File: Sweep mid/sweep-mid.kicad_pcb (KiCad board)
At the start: 2 copper layers, 229.5 x 95.2 mm, 62 parts, among them J1 AudioJack4dpb, J2 AudioJack4dpb, SW10 SW_Push, SW11 SW_Push, SW11_r1 SW_Push, SW12 SW_Push, SW12_r1 SW_Push, SW13_r1 SW_Push, SW14 SW_Push, SW15 SW_Push, SW15_r1 SW_Push, SW16 SW_Push, SW16_r1 SW_Push, SW17 SW_Push, SW17_r1 SW_Push, SW18 SW_Push, SW18_r1 SW_Push, SW2 SW_Push, SW2 SW_SPDT, SW20 SW_Push, SW20_r1 SW_Push, SW21 SW_Push, SW21_r1 SW_Push, SW2_r1 SW_Push, SW3 SW_Push, SW3_r1 SW_Push, SW4 SW_Push, SW4_r1 SW_Push, SW5 SW_Push, SW5_r1 SW_Push, SW6 SW_Push, SW6_r1 SW_Push, SW7_r1 SW_Push, SW8 SW_Push, SW8_r1 SW_Push, SW9 SW_Push, SW9_r1 SW_Push, U1 ProMicro-kbd, U2 ProMicro-kbd

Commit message: simplify footprint
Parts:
- SW10, SW11, SW11_r1, SW12, SW12_r1, SW13_r1, SW14, SW15, SW15_r1, SW16, SW16_r1, SW17, SW17_r1, SW18, SW18_r1, SW2, SW20, SW20_r1, SW21, SW21_r1, SW2_r1, SW3, SW3_r1, SW4, SW4_r1, SW5, SW5_r1, SW6, SW6_r1, SW7_r1, SW8, SW8_r1, SW9, SW9_r1: footprint mid:MXMountLP-1U -> sadik:gateron-ks27-choc-v1
- moved SW15 4.44 mm to (68.3, 102.1)
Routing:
- net Switch11: track 194.9 -> 156.7 mm
- net Switch1: track 170.7 -> 139.2 mm
- net Switch13: track 120.1 -> 89.0 mm
- net Switch12: track 148.7 -> 119.4 mm
- net Switch5: track 59.0 -> 30.8 mm
- net Switch4: track 80.8 -> 53.6 mm
- net Switch3: track 103.2 -> 78.3 mm
- net Switch14: track 102.0 -> 80.8 mm
- net Switch16: track 72.0 -> 51.9 mm
- net Switch15: track 63.1 -> 43.3 mm
- net Switch2: track 114.7 -> 95.5 mm
- net Switch9_r: track 103.2 -> 84.3 mm
- net Switch5_r: track 63.3 -> 45.1 mm
- net Switch4_r: track 84.8 -> 67.3 mm
- net Switch17_r: track 51.8 -> 35.0 mm
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
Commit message: routing
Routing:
- net Switch6: track 138.0 -> 103.1 mm
- net Switch9: track 66.3 -> 45.2 mm
- net Switch11: track 156.7 -> 151.6 mm
- net Switch12: track 119.4 -> 118.0 mm
- net Switch13: track 89.0 -> 87.6 mm
- net Switch8: track 84.2 -> 85.1 mm

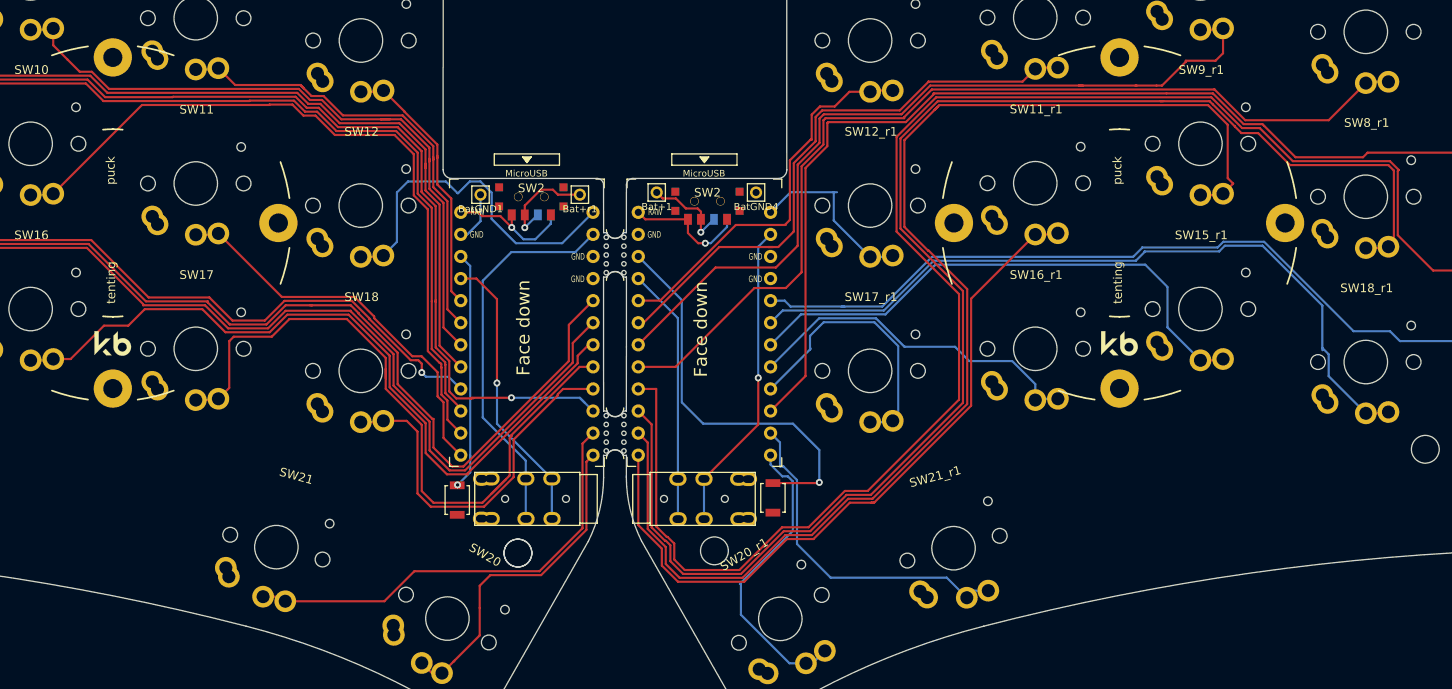
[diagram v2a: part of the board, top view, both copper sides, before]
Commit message: trrs only one way
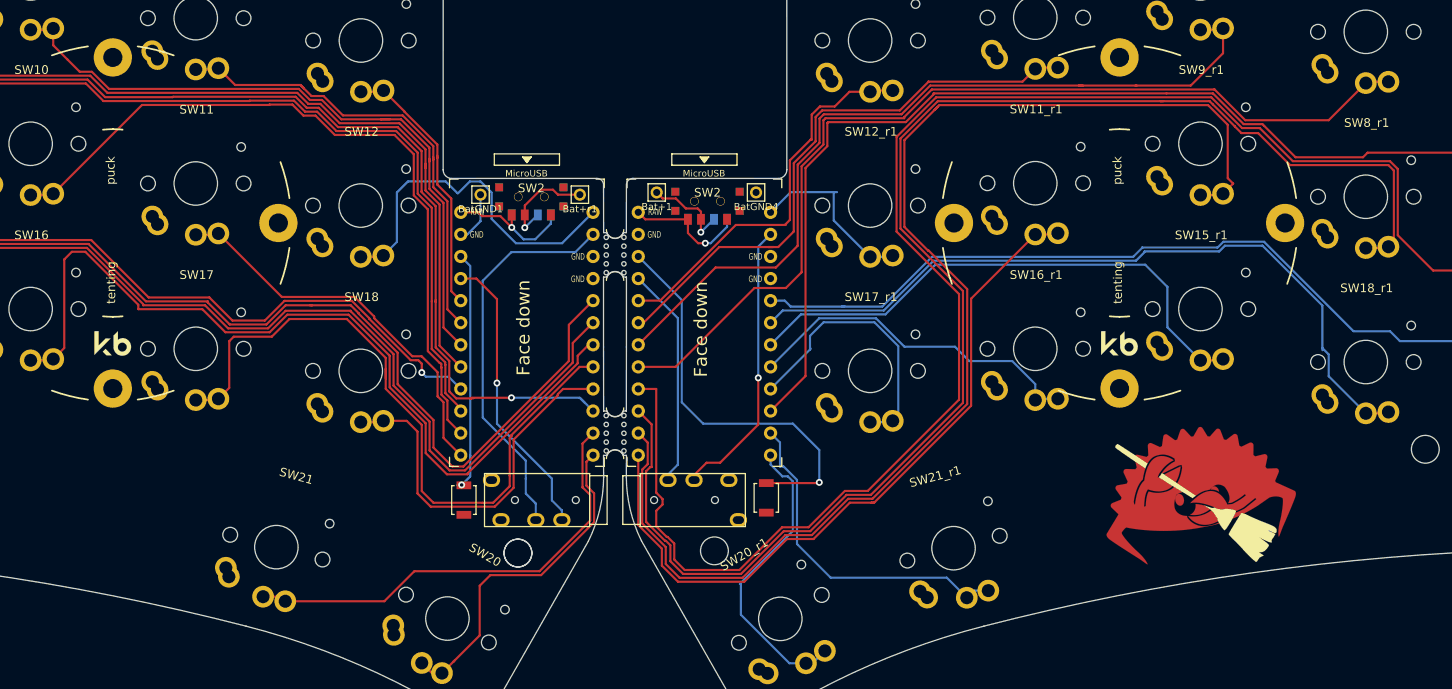
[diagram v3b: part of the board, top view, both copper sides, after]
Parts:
- added G***: LOGO, Kailh:ferris_broom, F.Cu at (216.1, 119.0)
- J1, J2: footprint Kailh:TRRS-PJ-DPB2 -> Kailh:TRRS-PJ-320A
- moved J1 1.15 mm to (153.1, 118.9)
- moved J2 1.14 mm to (147.3, 118.9)
- moved RSW1 0.76 mm to (132.8, 118.9)
- moved RSW2 0.76 mm to (167.6, 118.6)
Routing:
- net Switch13: track 87.6 -> 99.3 mm
- net vcc: track 62.7 -> 59.2 mm
- net Switch18_r: track 36.0 -> 32.8 mm
- net Switch14: track 80.5 -> 78.9 mm
- net gnd: track 12.4 -> 11.3 mm
- net Switch16: track 51.9 -> 52.6 mm
- net Switch17: track 38.7 -> 39.5 mm
- net Switch15: track 43.3 -> 44.0 mm
- net Switch7_r: track 168.5 -> 169.1 mm
- net Switch18: track 44.4 -> 45.0 mm
- net Switch8_r: track 145.1 -> 145.6 mm
- net Switch6_r: track 192.7 -> 193.2 mm

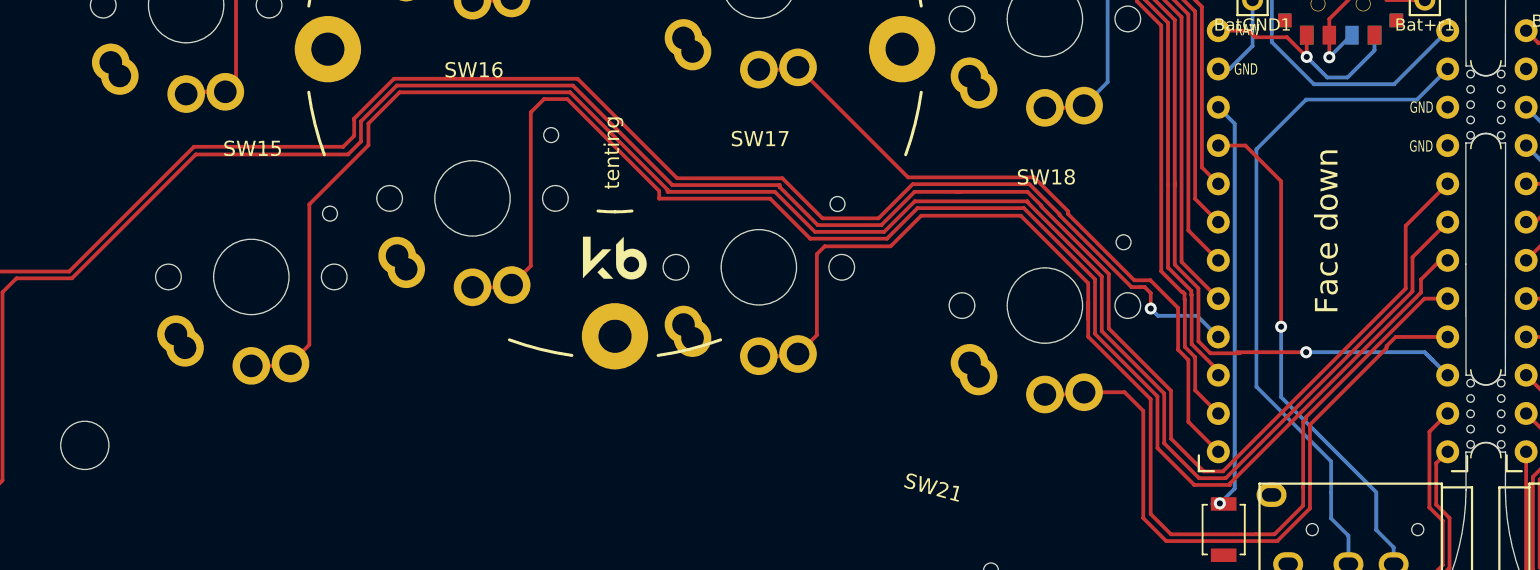
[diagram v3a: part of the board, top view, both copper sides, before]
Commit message: fix switch placement
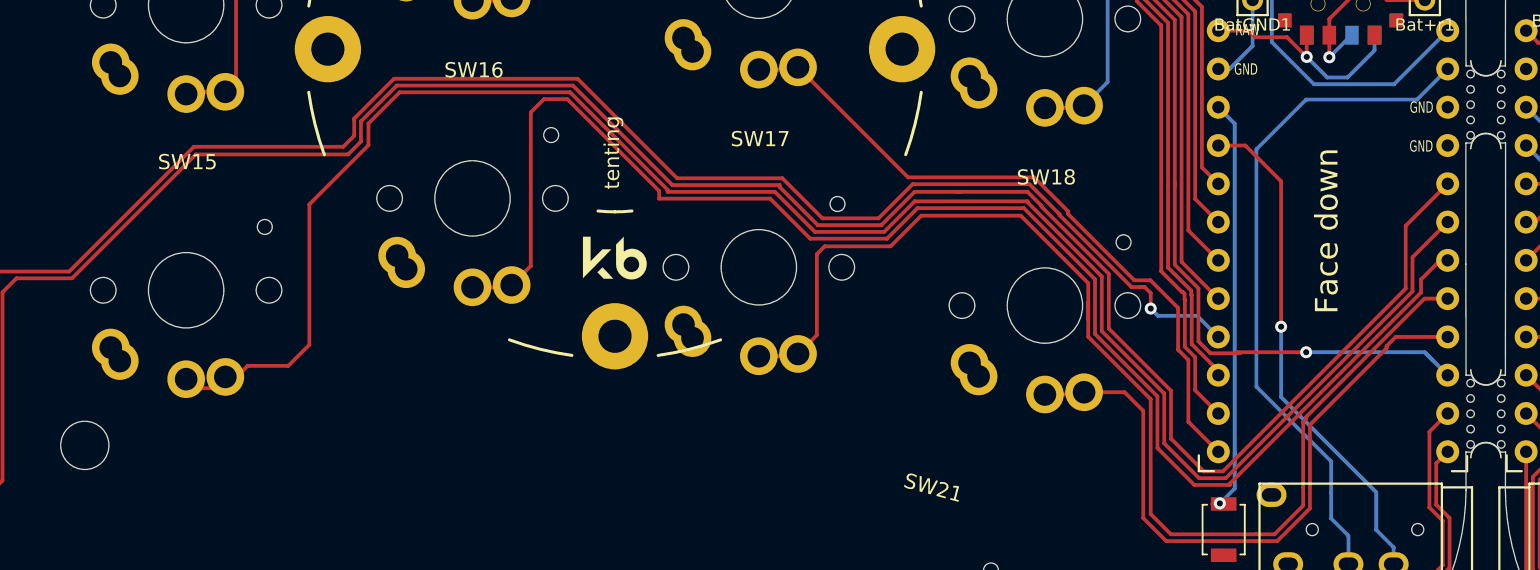
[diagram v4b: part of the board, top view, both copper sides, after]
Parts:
- moved SW15 4.42 mm to (64.0, 103.0)
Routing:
- net Switch12: track 118.0 -> 123.0 mm
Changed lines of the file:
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@@
   )
   (footprint "sadik:gateron-ks27-choc-v1" (layer "F.Cu")
-    (at 68.326 102.108)
+    (at 64 102.992)
     (attr through_hole)
     (fp_text reference "SW15" (at 0.1 -8.5 unlocked) (layer "F.SilkS")
@@
   (segment (start 110.128362 98.66896) (end 105.908678 98.66896) (width 0.25) (layer "F.Cu") (net 16))
   (segment (start 115.37448 96.46152) (end 119.829519 96.46152) (width 0.25) (layer "F.Cu") (net 16))
-  (segment (start 128.89694 109.845504) (end 128.89694 113.14894) (width 0.25) (layer "F.Cu") (net 17))
-  (segment (start 95.944197 96.46152) (end 103.06552 96.46152) (width 0.25) (layer "F.Cu") (net 17))
-  (segment (start 119.824141 97.091859) (end 119.824141 97.148341) (width 0.25) (layer "F.Cu") (net 17))
-  (segment (start 70.776 108.008) (end 70.926 107.858) (width 0.25) (layer "F.Cu") (net 17))
-  (segment (start 145.37001 100.80339) (end 147.7054 98.468) (width 0.25) (layer "F.Cu") (net 17))
-  (segment (start 110.31456 99.11848) (end 112.341182 97.091859) (width 0.25) (layer "F.Cu") (net 17))
-  (segment (start 103.06552 96.46152) (end 105.72248 99.11848) (width 0.25) (layer "F.Cu") (net 17))
-  (segment (start 89.475802 89.85752) (end 95.944197 96.325915) (width 0.25) (layer "F.Cu") (net 17))
-  (segment (start 72.175999 106.608001) (end 72.175999 97.290021) (width 0.25) (layer "F.Cu") (net 17))
-  (segment (start 76.09701 93.36901) (end 76.09701 91.924708) (width 0.25) (layer "F.Cu") (net 17))
-  (segment (start 132.977971 115.460601) (end 145.37001 103.068562) (width 0.25) (layer "F.Cu") (net 17))
-  (segment (start 145.37001 103.068562) (end 145.37001 100.80339) (width 0.25) (layer "F.Cu") (net 17))
-  (segment (start 95.944197 96.325915) (end 95.944197 96.46152) (width 0.25) (layer "F.Cu") (net 17))
-  (segment (start 131.208601 115.460601) (end 132.977971 115.460601) (width 0.25) (layer "F.Cu") (net 17))
-  (segment (start 124.753561 102.077761) (end 124.753561 105.702125) (width 0.25) (layer "F.Cu") (net 17))
-  (segment (start 68.326 108.008) (end 70.776 108.008) (width 0.25) (layer "F.Cu") (net 17))
-  (segment (start 124.753561 105.702125) (end 128.89694 109.845504) (width 0.25) (layer "F.Cu") (net 17))
-  (segment (start 70.926 107.858) (end 72.175999 106.608001) (width 0.25) (layer "F.Cu") (net 17))
-  (segment (start 128.89694 113.14894) (end 131.208601 115.460601) (width 0.25) (layer "F.Cu") (net 17))
-  (segment (start 72.175999 97.290021) (end 76.09701 93.36901) (width 0.25) (layer "F.Cu") (net 17))
-  (segment (start 119.824141 97.148341) (end 124.753561 102.077761) (width 0.25) (layer "F.Cu") (net 17))
-  (segment (start 78.164198 89.85752) (end 89.475802 89.85752) (width 0.25) (layer "F.Cu") (net 17))
-  (segment (start 105.72248 99.11848) (end 110.31456 99.11848) (width 0.25) (layer "F.Cu") (net 17))
-  (segment (start 112.341182 97.091859) (end 119.824141 97.091859) (width 0.25) (layer "F.Cu") (net 17))
-  (segment (start 76.09701 91.924708) (end 78.164198 89.85752) (width 0.25) (layer "F.Cu") (net 17))
+  (segment (start 131.208601 115.460601) (end 128.89694 113.14894) (width 0.25) (layer "F.Cu") (net 17))
+  (segment (start 70.776 108.008) (end 68.082 108.008) (width 0.25) (layer "F.Cu") (net 17))
+  (segment (start 119.824141 97.148341) (end 119.824141 97.091859) (width 0.25) (layer "F.Cu") (net 17))
+  (segment (start 124.753561 102.077761) (end 119.824141 97.148341) (width 0.25) (layer "F.Cu") (net 17))
+  (segment (start 110.31456 99.11848) (end 105.72248 99.11848) (width 0.25) (layer "F.Cu") (net 17))
+  (segment (start 95.944197 96.46152) (end 95.944197 96.325915) (width 0.25) (layer "F.Cu") (net 17))
+  (segment (start 128.89694 109.845504) (end 124.753561 105.702125) (width 0.25) (layer "F.Cu") (net 17))
+  (segment (start 68.082 108.008) (end 66.6 109.49) (width 0.25) (layer "F.Cu") (net 17))
+  (segment (start 95.944197 96.325915) (end 89.475802 89.85752) (width 0.25) (layer "F.Cu") (net 17))
+  (segment (start 78.164198 89.85752) (end 76.09701 91.924708) (width 0.25) (layer "F.Cu") (net 17))
+  (segment (start 89.475802 89.85752) (end 78.164198 89.85752) (width 0.25) (layer "F.Cu") (net 17))
+  (segment (start 103.06552 96.46152) (end 95.944197 96.46152) (width 0.25) (layer "F.Cu") (net 17))
+  (segment (start 76.09701 93.36901) (end 72.175999 97.290021) (width 0.25) (layer "F.Cu") (net 17))
+  (segment (start 119.824141 97.091859) (end 112.341182 97.091859) (width 0.25) (layer "F.Cu") (net 17))
+  (segment (start 105.72248 99.11848) (end 103.06552 96.46152) (width 0.25) (layer "F.Cu") (net 17))
+  (segment (start 72.175999 97.290021) (end 72.175999 106.608001) (width 0.25) (layer "F.Cu") (net 17))
+  (segment (start 66.6 109.49) (end 64.15 109.49) (width 0.25) (layer "F.Cu") (net 17))
+  (segment (start 145.37001 103.068562) (end 132.977971 115.460601) (width 0.25) (layer "F.Cu") (net 17))
+  (segment (start 76.09701 91.924708) (end 76.09701 93.36901) (width 0.25) (layer "F.Cu") (net 17))
+  (segment (start 124.753561 105.702125) (end 124.753561 102.077761) (width 0.25) (layer "F.Cu") (net 17))
+  (segment (start 147.7054 98.468) (end 145.37001 100.80339) (width 0.25) (layer "F.Cu") (net 17))
+  (segment (start 112.341182 97.091859) (end 110.31456 99.11848) (width 0.25) (layer "F.Cu") (net 17))
+  (segment (start 128.89694 113.14894) (end 128.89694 109.845504) (width 0.25) (layer "F.Cu") (net 17))
+  (segment (start 145.37001 100.80339) (end 145.37001 103.068562) (width 0.25) (layer "F.Cu") (net 17))
+  (segment (start 72.175999 106.608001) (end 70.776 108.008) (width 0.25) (layer "F.Cu") (net 17))
+  (segment (start 132.977971 115.460601) (end 131.208601 115.460601) (width 0.25) (layer "F.Cu") (net 17))
+  (segment (start 64.15 109.49) (end 64 109.64) (width 0.25) (layer "F.Cu") (net 17))
   (segment (start 89.289604 90.30704) (end 95.38704 96.404476) (width 0.25) (layer "F.Cu") (net 18))
   (segment (start 85.6 102.646) (end 86.868 101.378) (width 0.25) (layer "F.Cu") (net 18))
